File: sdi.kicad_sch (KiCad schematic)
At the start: 50 parts, among them J2 031-70526-21, J3 031-70526-21, U11 LIFCL-40-9BG256C, U15 GS2971A, U16 GS2988, Y1 ABM7_27.000MH_D2Y_T

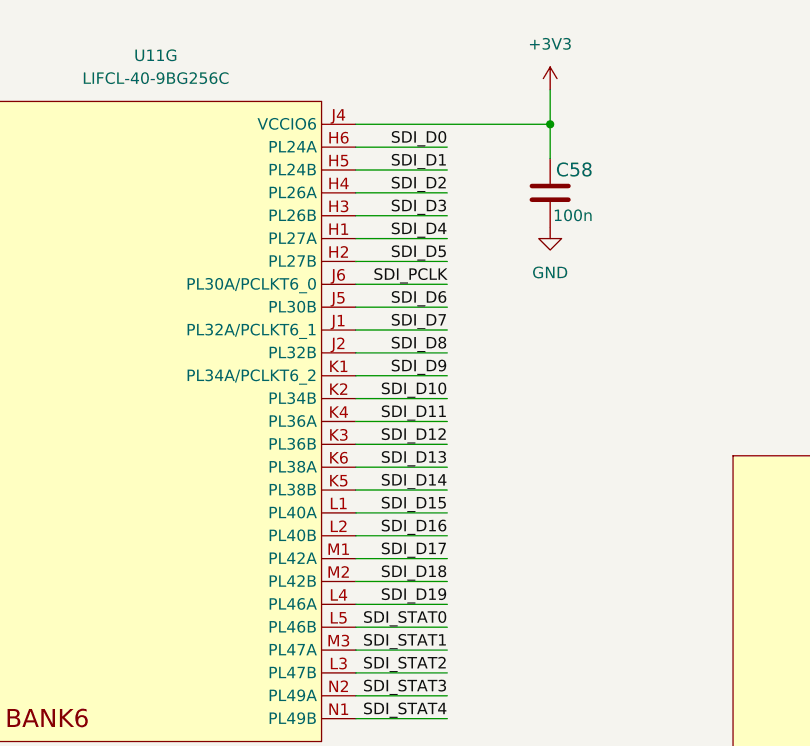
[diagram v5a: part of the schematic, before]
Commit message: Routed SDI data interface
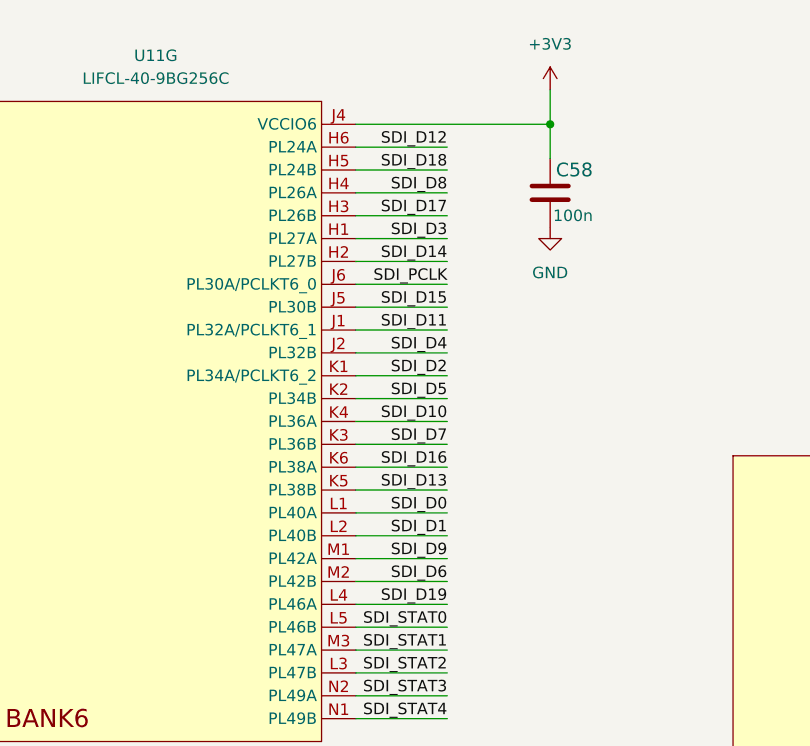
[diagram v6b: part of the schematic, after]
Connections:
- net SDI_D0: now also U11.L1 (PL40A); no longer U11.H6 (PL24A)
- net SDI_D1: now also U11.L2 (PL40B); no longer U11.H5 (PL24B)
- net SDI_D10: now also U11.K4 (PL36A); no longer U11.K2 (PL34B)
- net SDI_D11: now also U11.J1 (PL32A/PCLKT6_1); no longer U11.K4 (PL36A)
- net SDI_D12: now also U11.H6 (PL24A); no longer U11.K3 (PL36B)
- net SDI_D13: now also U11.K5 (PL38B); no longer U11.K6 (PL38A)
- net SDI_D14: now also U11.H2 (PL27B); no longer U11.K5 (PL38B)
- net SDI_D15: now also U11.J5 (PL30B); no longer U11.L1 (PL40A)
- net SDI_D16: now also U11.K6 (PL38A); no longer U11.L2 (PL40B)
- net SDI_D17: now also U11.H3 (PL26B); no longer U11.M1 (PL42A)
- net SDI_D18: now also U11.H5 (PL24B); no longer U11.M2 (PL42B)
- net SDI_D2: now also U11.K1 (PL34A/PCLKT6_2); no longer U11.H4 (PL26A)
- net SDI_D3: now also U11.H1 (PL27A); no longer U11.H3 (PL26B)
- net SDI_D4: now also U11.J2 (PL32B); no longer U11.H1 (PL27A)
- net SDI_D5: now also U11.K2 (PL34B); no longer U11.H2 (PL27B)
- net SDI_D6: now also U11.M2 (PL42B); no longer U11.J5 (PL30B)
- net SDI_D7: now also U11.K3 (PL36B); no longer U11.J1 (PL32A/PCLKT6_1)
- net SDI_D8: now also U11.H4 (PL26A); no longer U11.J2 (PL32B)
- net SDI_D9: now also U11.M1 (PL42A); no longer U11.K1 (PL34A/PCLKT6_2)
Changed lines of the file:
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@@
     (effects (font (size 4 4)) (justify left bottom))
   )
-  (label "SDI_D12" (at 106.68 59.69 180)
+  (label "SDI_D12" (at 106.68 26.67 180)
     (effects (font (size 1.27 1.27)) (justify right bottom))
   )
@@
     (effects (font (size 1.27 1.27)) (justify left bottom))
   )
-  (label "SDI_D18" (at 106.68 74.93 180)
+  (label "SDI_D18" (at 106.68 29.21 180)
     (effects (font (size 1.27 1.27)) (justify right bottom))
   )
@@
     (effects (font (size 1.27 1.27)) (justify right bottom))
   )
-  (label "SDI_D16" (at 106.68 69.85 180)
+  (label "SDI_D16" (at 106.68 62.23 180)
     (effects (font (size 1.27 1.27)) (justify right bottom))
   )
@@
     (effects (font (size 1.27 1.27)) (justify right bottom))
   )
-  (label "SDI_D15" (at 106.68 67.31 180)
+  (label "SDI_D15" (at 106.68 44.45 180)
     (effects (font (size 1.27 1.27)) (justify right bottom))
   )
@@
     (effects (font (size 1.27 1.27)) (justify left bottom))
   )
-  (label "SDI_D3" (at 106.68 34.29 180)
-    (effects (font (size 1.27 1.27)) (justify right bottom))
-  )
-  (label "SDI_D4" (at 106.68 36.83 180)
-    (effects (font (size 1.27 1.27)) (justify right bottom))
-  )
-  (label "SDI_D17" (at 106.68 72.39 180)
+  (label "SDI_D3" (at 106.68 36.83 180)
+    (effects (font (size 1.27 1.27)) (justify right bottom))
+  )
+  (label "SDI_D4" (at 106.68 49.53 180)
+    (effects (font (size 1.27 1.27)) (justify right bottom))
+  )
+  (label "SDI_D17" (at 106.68 34.29 180)
     (effects (font (size 1.27 1.27)) (justify right bottom))
   )
@@
     (effects (font (size 1.27 1.27)) (justify left bottom))
   )
-  (label "SDI_D5" (at 106.68 39.37 180)
-    (effects (font (size 1.27 1.27)) (justify right bottom))
-  )
-  (label "SDI_D9" (at 106.68 52.07 180)
+  (label "SDI_D5" (at 106.68 54.61 180)
+    (effects (font (size 1.27 1.27)) (justify right bottom))
+  )
+  (label "SDI_D9" (at 106.68 72.39 180)
     (effects (font (size 1.27 1.27)) (justify right bottom))
   )
@@
     (effects (font (size 1.27 1.27)) (justify left bottom))
   )
-  (label "SDI_D14" (at 106.68 64.77 180)
-    (effects (font (size 1.27 1.27)) (justify right bottom))
-  )
-  (label "SDI_D10" (at 106.68 54.61 180)
+  (label "SDI_D14" (at 106.68 39.37 180)
+    (effects (font (size 1.27 1.27)) (justify right bottom))
+  )
+  (label "SDI_D10" (at 106.68 57.15 180)
     (effects (font (size 1.27 1.27)) (justify right bottom))
   )
@@
     (effects (font (size 1.27 1.27)) (justify right bottom))
   )
-  (label "SDI_D7" (at 106.68 46.99 180)
+  (label "SDI_D7" (at 106.68 59.69 180)
     (effects (font (size 1.27 1.27)) (justify right bottom))
   )
@@
     (effects (font (size 1.27 1.27)) (justify left bottom))
   )
-  (label "SDI_D8" (at 106.68 49.53 180)
+  (label "SDI_D8" (at 106.68 31.75 180)
     (effects (font (size 1.27 1.27)) (justify right bottom))
   )
@@
     (effects (font (size 1.27 1.27)) (justify left bottom))
   )
-  (label "SDI_D2" (at 106.68 31.75 180)
+  (label "SDI_D2" (at 106.68 52.07 180)
     (effects (font (size 1.27 1.27)) (justify right bottom))
   )
@@
     (effects (font (size 1.27 1.27)) (justify left bottom))
   )
-  (label "SDI_D11" (at 106.68 57.15 180)
+  (label "SDI_D11" (at 106.68 46.99 180)
     (effects (font (size 1.27 1.27)) (justify right bottom))
   )
@@
     (effects (font (size 1.27 1.27)) (justify right bottom))
   )
-  (label "SDI_D0" (at 106.68 26.67 180)
-    (effects (font (size 1.27 1.27)) (justify right bottom))
-  )
-  (label "SDI_D6" (at 106.68 44.45 180)
+  (label "SDI_D0" (at 106.68 67.31 180)
+    (effects (font (size 1.27 1.27)) (justify right bottom))
+  )
+  (label "SDI_D6" (at 106.68 74.93 180)
     (effects (font (size 1.27 1.27)) (justify right bottom))
   )
@@
     (effects (font (size 1.27 1.27)) (justify left bottom))
   )
-  (label "SDI_D13" (at 106.68 62.23 180)
+  (label "SDI_D13" (at 106.68 64.77 180)
     (effects (font (size 1.27 1.27)) (justify right bottom))
   )
@@
     (effects (font (size 1.27 1.27)) (justify right bottom))
   )
-  (label "SDI_D1" (at 106.68 29.21 180)
-    (effects (font (size 1.27 1.27)) (justify right bottom))
-  )
+  (label "SDI_D1" (at 106.68 69.85 180)
+    (effects (font (size 1.27 1.27)) (justify right bottom))
+  )

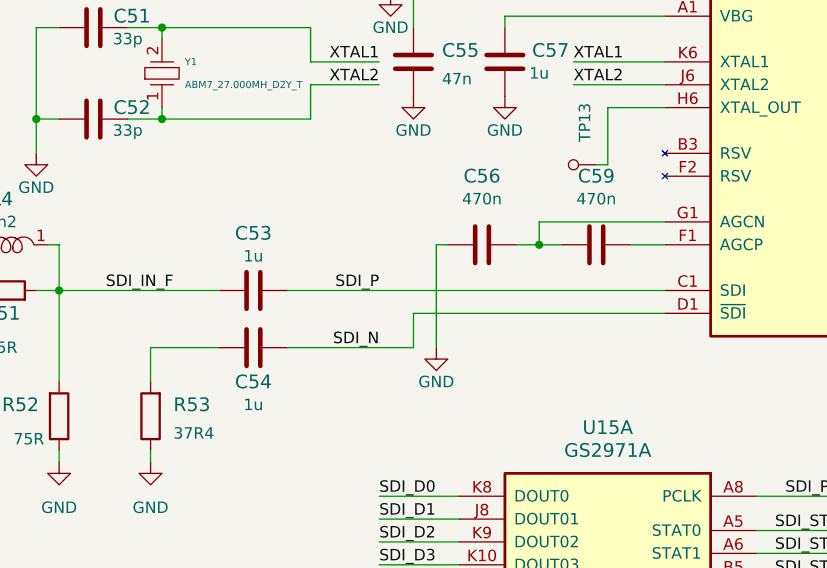
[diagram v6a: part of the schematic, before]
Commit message: Length matched most high speed interfaces
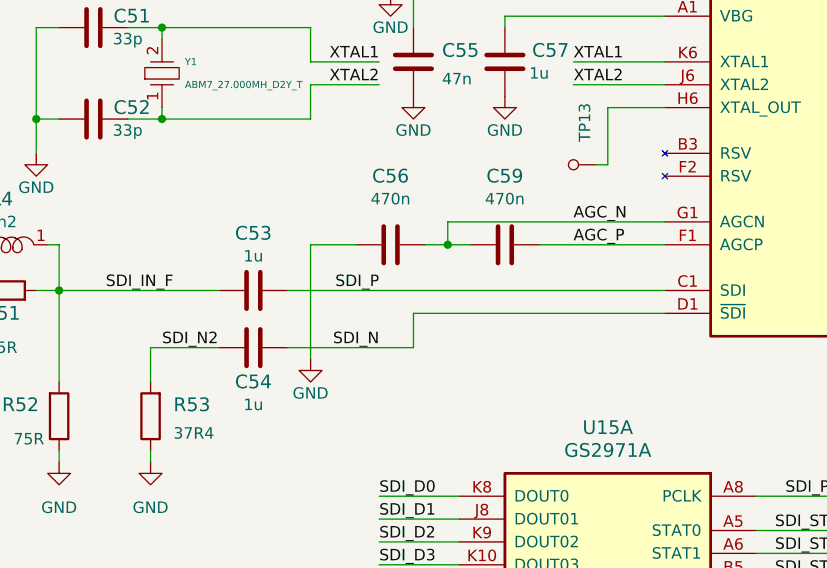
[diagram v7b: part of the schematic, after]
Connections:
- net AGC_N: now reaches C56.2, C59.1, U15.G1 (AGCN)
- net AGC_P: now reaches C59.2, U15.F1 (AGCP)
- net SDI_N2: now reaches C54.1, R53.2
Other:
- moved on the sheet: C56, C59
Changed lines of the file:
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@@
   (junction (at 43.18 203.2) (diameter 0) (color 0 0 0 0)
   )
-  (junction (at 109.22 198.12) (diameter 0) (color 0 0 0 0)
+  (junction (at 99.06 198.12) (diameter 0) (color 0 0 0 0)
   )
   (junction (at 283.21 229.87) (diameter 0) (color 0 0 0 0)
@@
     (stroke (width 0) (type default) (color 0 0 0 0))
   )
-  (wire (pts (xy 119.38 198.12) (xy 123.19 198.12))
+  (wire (pts (xy 109.22 198.12) (xy 123.19 198.12))
     (stroke (width 0) (type default) (color 0 0 0 0))
   )
@@
     (stroke (width 0) (type default) (color 0 0 0 0))
   )
-  (wire (pts (xy 97.79 198.12) (xy 97.79 209.55))
-    (stroke (width 0) (type default) (color 0 0 0 0))
-  )
   (wire (pts (xy 228.6 251.46) (xy 228.6 252.73))
     (stroke (width 0) (type default) (color 0 0 0 0))
@@
     (stroke (width 0) (type default) (color 0 0 0 0))
   )
-  (wire (pts (xy 106.68 198.12) (xy 109.22 198.12))
+  (wire (pts (xy 96.52 198.12) (xy 99.06 198.12))
     (stroke (width 0) (type default) (color 0 0 0 0))
   )
@@
     (stroke (width 0) (type default) (color 0 0 0 0))
   )
-  (wire (pts (xy 109.22 198.12) (xy 111.76 198.12))
+  (wire (pts (xy 99.06 198.12) (xy 101.6 198.12))
     (stroke (width 0) (type default) (color 0 0 0 0))
   )
-  (wire (pts (xy 109.22 195.58) (xy 109.22 198.12))
+  (wire (pts (xy 99.06 195.58) (xy 99.06 198.12))
     (stroke (width 0) (type default) (color 0 0 0 0))
   )
@@
     (stroke (width 0) (type default) (color 0 0 0 0))
   )
+  (wire (pts (xy 83.82 210.82) (xy 83.82 198.12))
+    (stroke (width 0) (type default) (color 0 0 0 0))
+  )
   (wire (pts (xy 289.56 55.88) (xy 289.56 54.61))
     (stroke (width 0) (type default) (color 0 0 0 0))
@@
     (stroke (width 0) (type default) (color 0 0 0 0))
   )
-  (wire (pts (xy 123.19 195.58) (xy 109.22 195.58))
-    (stroke (width 0) (type default) (color 0 0 0 0))
-  )
   (wire (pts (xy 280.67 233.68) (xy 283.21 233.68))
     (stroke (width 0) (type default) (color 0 0 0 0))
@@
     (stroke (width 0) (type default) (color 0 0 0 0))
   )
+  (wire (pts (xy 99.06 195.58) (xy 123.19 195.58))
+    (stroke (width 0) (type default) (color 0 0 0 0))
+  )
   (wire (pts (xy 281.94 100.33) (xy 281.94 101.6))
     (stroke (width 0) (type default) (color 0 0 0 0))
@@
     (stroke (width 0) (type default) (color 0 0 0 0))
   )
-  (wire (pts (xy 99.06 198.12) (xy 97.79 198.12))
+  (wire (pts (xy 83.82 198.12) (xy 88.9 198.12))
     (stroke (width 0) (type default) (color 0 0 0 0))
   )
@@
     (effects (font (size 1.27 1.27)) (justify left bottom))
   )
+  (label "SDI_N2" (at 67.31 209.55 0)
+    (effects (font (size 1.27 1.27)) (justify left bottom))
+  )
   (label "SW_EN" (at 180.34 200.66 180)
     (effects (font (size 1.27 1.27)) (justify right bottom))
@@
     (effects (font (size 1.27 1.27)) (justify right bottom))
   )
+  (label "AGC_N" (at 113.03 195.58 0)
+    (effects (font (size 1.27 1.27)) (justify left bottom))
+  )
   (label "SDI_OUT_P" (at 321.31 95.25 0)
     (effects (font (size 1.27 1.27)) (justify left bottom))
@@
     (effects (font (size 1.27 1.27)) (justify right bottom))
   )
+  (label "AGC_P" (at 113.03 198.12 0)
+    (effects (font (size 1.27 1.27)) (justify left bottom))
+  )
   (label "~{CS_TMS}" (at 110.49 119.38 180)
     (effects (font (size 1.27 1.27)) (justify right bottom))
@@
     (pin "2")
   )
-  (symbol (lib_id "crosslink-nx-video-converter:C_470n_0402") (at 115.57 198.12 90) (unit 1)
+  (symbol (lib_id "crosslink-nx-video-converter:C_470n_0402") (at 105.41 198.12 90) (unit 1)
     (in_bom yes) (on_board yes) (fields_autoplaced)
-    (property "Reference" "C59" (id 0) (at 115.57 190.5 90)
+    (property "Reference" "C59" (id 0) (at 105.41 190.5 90)
       (effects (font (size 1.524 1.524)))
     )
-    (property "Value" "C_470n_0402" (id 1) (at 119.38 198.12 0)
+    (property "Value" "C_470n_0402" (id 1) (at 109.22 198.12 0)
       (effects (font (size 1.524 1.524)) hide)
     )
-    (property "Footprint" "crosslink-nx-video-converter-footprints:0402-cap" (id 2) (at 110.49 193.04 0)
+    (property "Footprint" "crosslink-nx-video-converter-footprints:0402-cap" (id 2) (at 100.33 193.04 0)
       (effects (font (size 1.524 1.524)) (justify left) hide)
     )
-    (property "Datasheet" "" (id 3) (at 115.57 198.12 0)
+    (property "Datasheet" "" (id 3) (at 105.41 198.12 0)
       (effects (font (size 1.27 1.27)) hide)
     )
-    (property "Manufacturer" "TDK" (id 4) (at 105.41 193.04 0)
+    (property "Manufacturer" "TDK" (id 4) (at 95.25 193.04 0)
       (effects (font (size 1.524 1.524)) (justify left) hide)
     )
-    (property "MPN" "C1005X5R1E474M050BB" (id 5) (at 107.95 193.04 0)
+    (property "MPN" "C1005X5R1E474M050BB" (id 5) (at 97.79 193.04 0)
       (effects (font (size 1.524 1.524)) (justify left) hide)
     )
-    (property "Val" "470n" (id 6) (at 115.57 193.04 90))
+    (property "Val" "470n" (id 6) (at 105.41 193.04 90))
     (pin "1")
     (pin "2")
@@
     (pin "2")
   )
-  (symbol (lib_id "crosslink-nx-video-converter:GND") (at 97.79 209.55 0) (unit 1)
+  (symbol (lib_id "crosslink-nx-video-converter:GND") (at 83.82 210.82 0) (unit 1)
     (in_bom yes) (on_board yes)
-    (property "Reference" "#PWR0112" (id 0) (at 97.79 215.9 0)
+    (property "Reference" "#PWR0112" (id 0) (at 83.82 217.17 0)
       (effects (font (size 1.27 1.27)) hide)
     )
-    (property "Value" "GND" (id 1) (at 97.79 213.36 0))
-    (property "Footprint" "crosslink-nx-video-converter-footprints:" (id 2) (at 97.79 209.55 0)
+    (property "Value" "GND" (id 1) (at 83.82 214.63 0))
+    (property "Footprint" "crosslink-nx-video-converter-footprints:" (id 2) (at 83.82 210.82 0)
       (effects (font (size 1.27 1.27)) hide)
     )
-    (property "Datasheet" "" (id 3) (at 97.79 209.55 0)
+    (property "Datasheet" "" (id 3) (at 83.82 210.82 0)
       (effects (font (size 1.27 1.27)) hide)
     )
@@
     (pin "2")
   )
-  (symbol (lib_id "crosslink-nx-video-converter:C_470n_0402") (at 102.87 198.12 90) (unit 1)
+  (symbol (lib_id "crosslink-nx-video-converter:C_470n_0402") (at 92.71 198.12 90) (unit 1)
     (in_bom yes) (on_board yes) (fields_autoplaced)
-    (property "Reference" "C56" (id 0) (at 102.87 190.5 90)
+    (property "Reference" "C56" (id 0) (at 92.71 190.5 90)
       (effects (font (size 1.524 1.524)))
     )
-    (property "Value" "C_470n_0402" (id 1) (at 106.68 198.12 0)
+    (property "Value" "C_470n_0402" (id 1) (at 96.52 198.12 0)
       (effects (font (size 1.524 1.524)) hide)
     )
-    (property "Footprint" "crosslink-nx-video-converter-footprints:0402-cap" (id 2) (at 97.79 193.04 0)
+    (property "Footprint" "crosslink-nx-video-converter-footprints:0402-cap" (id 2) (at 87.63 193.04 0)
       (effects (font (size 1.524 1.524)) (justify left) hide)
     )
-    (property "Datasheet" "" (id 3) (at 102.87 198.12 0)
+    (property "Datasheet" "" (id 3) (at 92.71 198.12 0)
       (effects (font (size 1.27 1.27)) hide)
     )
-    (property "Manufacturer" "TDK" (id 4) (at 92.71 193.04 0)
+    (property "Manufacturer" "TDK" (id 4) (at 82.55 193.04 0)
       (effects (font (size 1.524 1.524)) (justify left) hide)
     )
-    (property "MPN" "C1005X5R1E474M050BB" (id 5) (at 95.25 193.04 0)
+    (property "MPN" "C1005X5R1E474M050BB" (id 5) (at 85.09 193.04 0)
       (effects (font (size 1.524 1.524)) (justify left) hide)
     )
-    (property "Val" "470n" (id 6) (at 102.87 193.04 90))
+    (property "Val" "470n" (id 6) (at 92.71 193.04 90))
     (pin "1")
     (pin "2")

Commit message: Added testpoints and LEDs for SDI circuitry
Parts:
- added D? (x2): LTST-C190GKT, crosslink-nx-video-converter-footprints:LED_0603, symbol crosslink-nx-video-converter:LTST-C190GKT
- added R? (x2): R_200R_0603, antmicro-footprints:0603-res, symbol antmicroResistors0603:R_200R_0603
- added TP? (x20): TP_SMD_0_75MM, crosslink-nx-video-converter-footprints:Testpoint_smd_0_75mm, symbol crosslink-nx-video-converter:TP_SMD_0_75MM
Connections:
- net 20bit/~{10bit}: now also TP?.1
- net AUDIO_EN/~{DIS}: now also TP?.1
- net DVB_ASI: now also TP?.1
- net GND: now also D?.2, D?.2
- net IOPROC_EN/~{DIS}: now also TP?.1
- net JTAG/~{HOST}: now also TP?.1
- net RESET_TRST: now also TP?.1
- net SCLK_TCK: now also TP?.1
- net SDIN_TDI: now also TP?.1
- net SDI_STAT0: now also TP?.1
- net SDI_STAT1: now also TP?.1
- net SDI_STAT2: now also TP?.1
- net SDI_STAT3: now also R?.2
- net SDI_STAT4: now also TP?.1
- net SDI_STAT5: now also R?.2
- net SDOUT_TDO: now also TP?.1
- net SDO_EN/DIS: now also TP?.1
- net STANDBY: now also TP?.1
- net SW_EN: now also TP?.1
- net TIM_861: now also TP?.1
- net ~{CS_TMS}: now also TP?.1
- net ~{RC_BYP}: now also TP?.1
- net ~{SMPTE_BYPASS}: now also TP?.1
- new net: D?.1, R?.1 (x2)
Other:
- moved on the sheet: C51, C52, C53, C54, C55, C56, C57, C59, C60, C61, C62, C63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
